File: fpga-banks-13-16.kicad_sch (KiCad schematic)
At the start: 40 parts, among them U14 XC7A100T-FGG484, U15 AMJMEFB-100.0000T

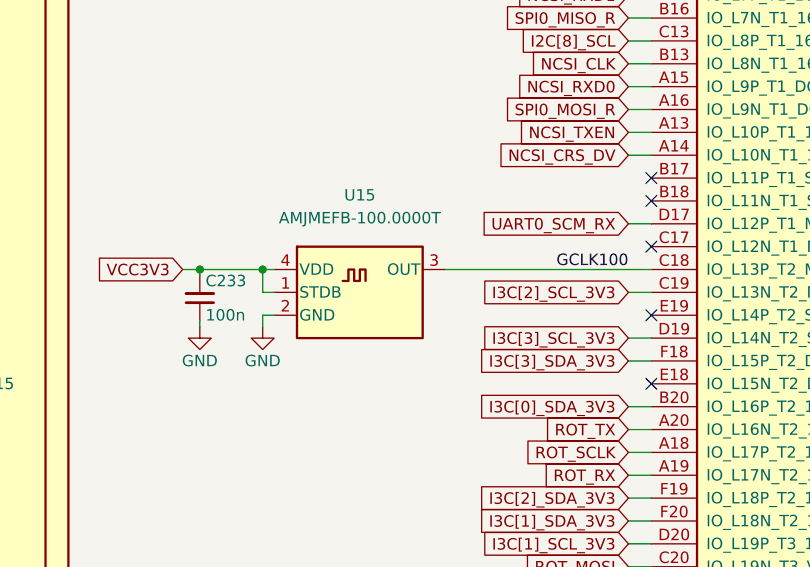
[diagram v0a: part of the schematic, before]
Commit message: [#55652] Fix hotareas
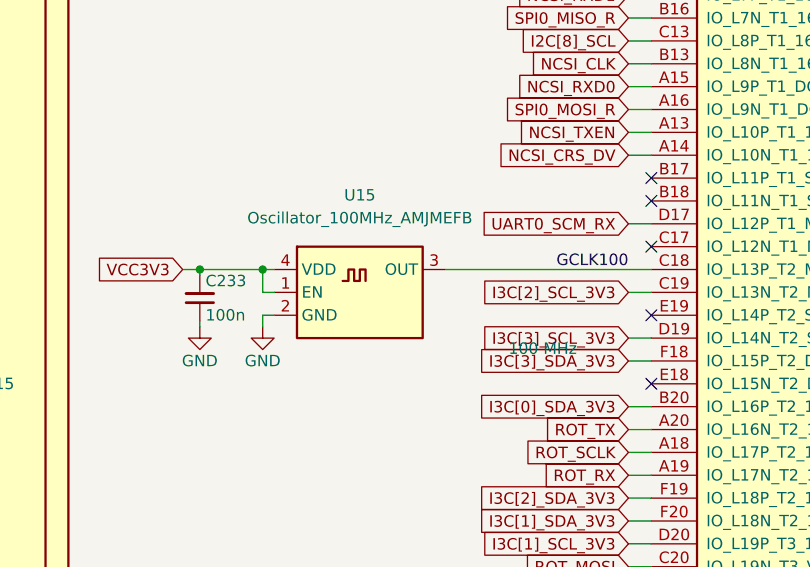
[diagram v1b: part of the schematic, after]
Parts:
- U14: footprint antmicro-footprints:BGA-484_23x23mm_Layout22x22_P1mm_Xilinx_FGG484 -> antmicro-footprints:BGA-484_23x23mm_Layout22x22_P1mm_FGG484; symbol antmicroMicrocontrollers:XC7A100T-FGG484 -> antmicroFPGAChips:XC7A100T-FGG484; Manufacturer Xilinx -> AMD-Xilinx
- U15: value AMJMEFB-100.0000T -> Oscillator_100MHz_AMJMEFB; symbol antmicroOscillators:AMJMEFB-100.0000T -> antmicroOscillators:Oscillator_100MHz_AMJMEFB; Val (none) -> 100 MHz

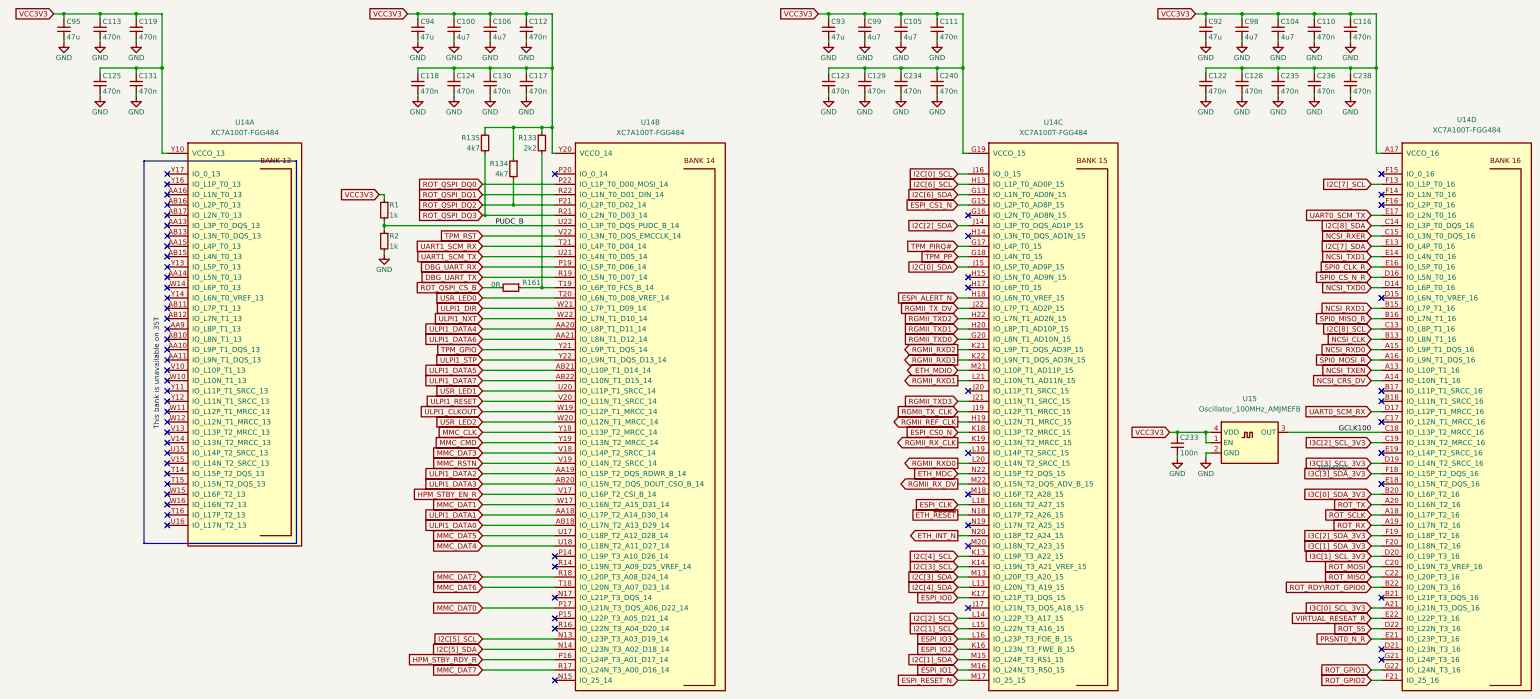
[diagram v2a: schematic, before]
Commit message: [#68236] Allign sch to grid
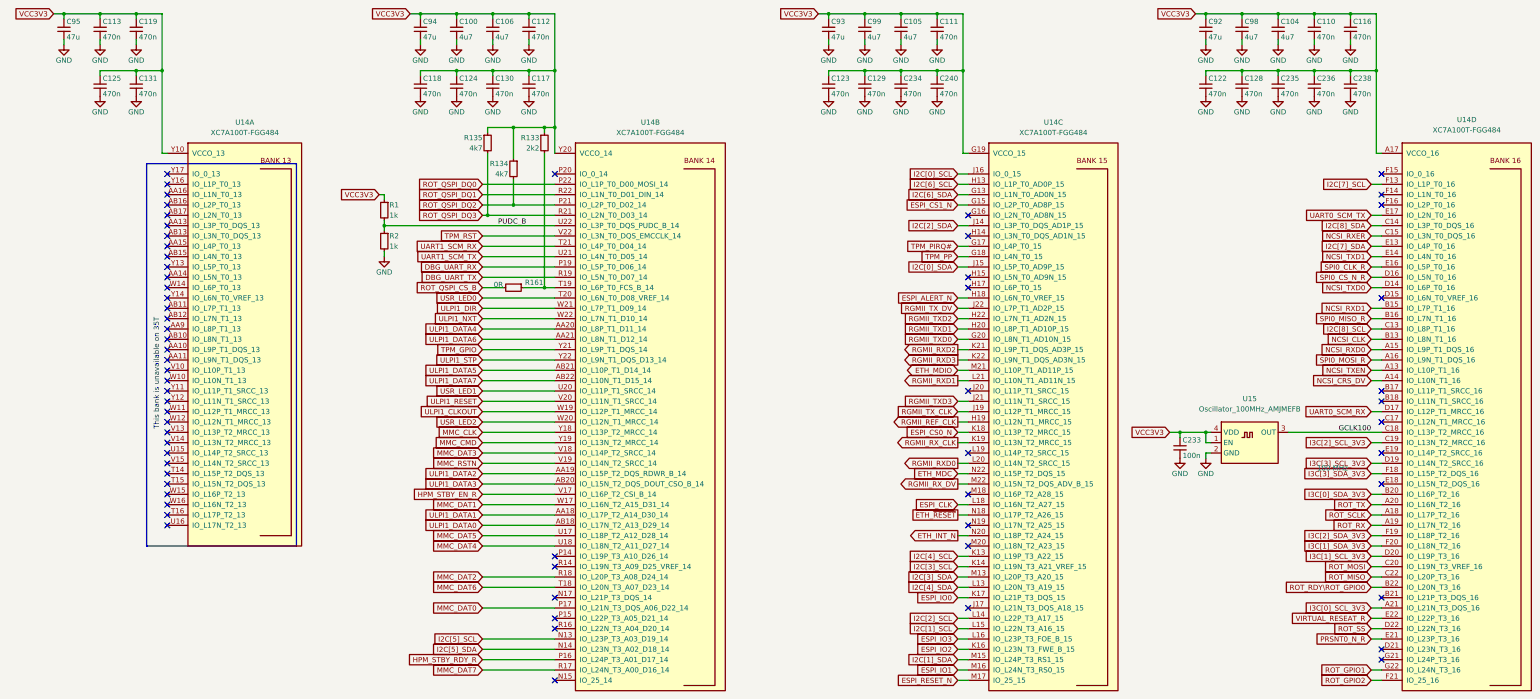
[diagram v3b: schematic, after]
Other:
- moved on the sheet: C100, C106, C112, C117, C118, C122, C123, C124, C125, C128, C129, C130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

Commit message: [#68236] Remove DNP property from Testpoints
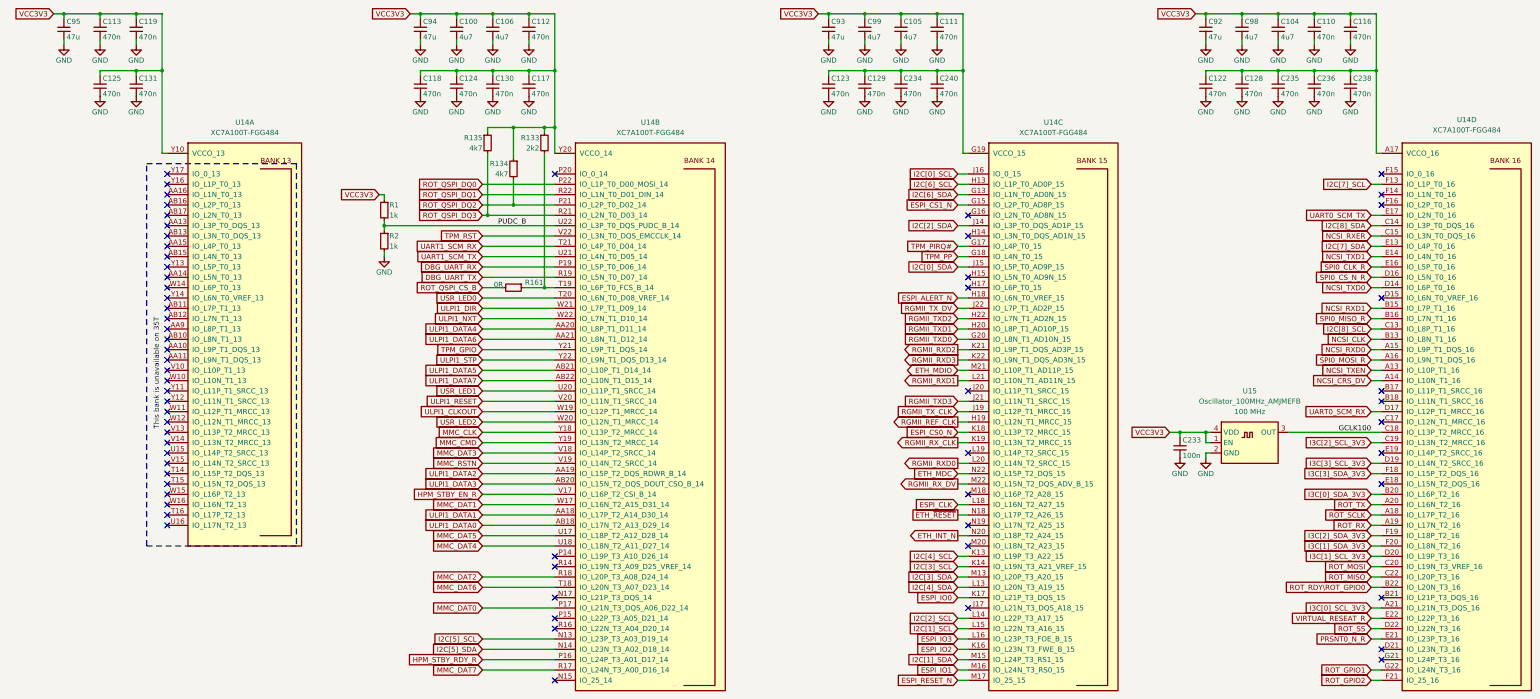
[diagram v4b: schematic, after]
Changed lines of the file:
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@@
   )
   (polyline (pts (xy 53.34 87.63) (xy 90.17 87.63))
-    (stroke (width 0) (type default))
+    (stroke (width 0) (type dash))
   )
   (wire (pts (xy 153.67 209.55) (xy 135.89 209.55))
@@
   )
   (polyline (pts (xy 90.17 87.63) (xy 90.17 181.61))
-    (stroke (width 0) (type default))
+    (stroke (width 0) (type dash))
   )
   (wire (pts (xy 50.8 57.15) (xy 50.8 58.42))
@@
   )
   (polyline (pts (xy 53.34 181.61) (xy 53.34 87.63))
-    (stroke (width 0) (type default))
+    (stroke (width 0) (type dash))
   )
   (wire (pts (xy 322.58 64.77) (xy 331.47 64.77))
@@
   )
   (polyline (pts (xy 90.17 181.61) (xy 53.34 181.61))
-    (stroke (width 0) (type default))
+    (stroke (width 0) (type dash))
   )
   (wire (pts (xy 120.65 50.8) (xy 120.65 52.07))
@@
   (symbol (lib_id "antmicroOscillators:Oscillator_100MHz_AMJMEFB") (at 314.96 153.67 0) (unit 1)
     (in_bom yes) (on_board yes) (dnp no) (fields_autoplaced)
-    (property "Reference" "U15" (at 324.485 145.415 0)
+    (property "Reference" "U15" (at 324.485 143.51 0)
       (effects (font (size 1.27 1.27)))
     )
-    (property "Value" "Oscillator_100MHz_AMJMEFB" (at 324.485 147.955 0)
+    (property "Value" "Oscillator_100MHz_AMJMEFB" (at 324.485 146.05 0)
       (effects (font (size 1.27 1.27)))
     )
@@
       (effects (font (size 1.27 1.27) (thickness 0.15)) (justify left bottom) hide)
     )
-    (property "Val" "100 MHz" (at 340.995 163.195 0)
-      (effects (font (size 1.27 1.27) (thickness 0.15)) (justify left bottom))
+    (property "Val" "100 MHz" (at 324.485 148.59 0)
+      (effects (font (size 1.27 1.27) (thickness 0.15)))
     )
     (pin "1")
